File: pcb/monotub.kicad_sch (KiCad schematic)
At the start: 39 parts, among them J1 Barrel_Jack, J2 SCD-40, J3 PROG, J4 FAN, J5 HUMID, J6 WLVL, J7 PUMP, J8 RGB, Q1 NMOS, Q2 NMOS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

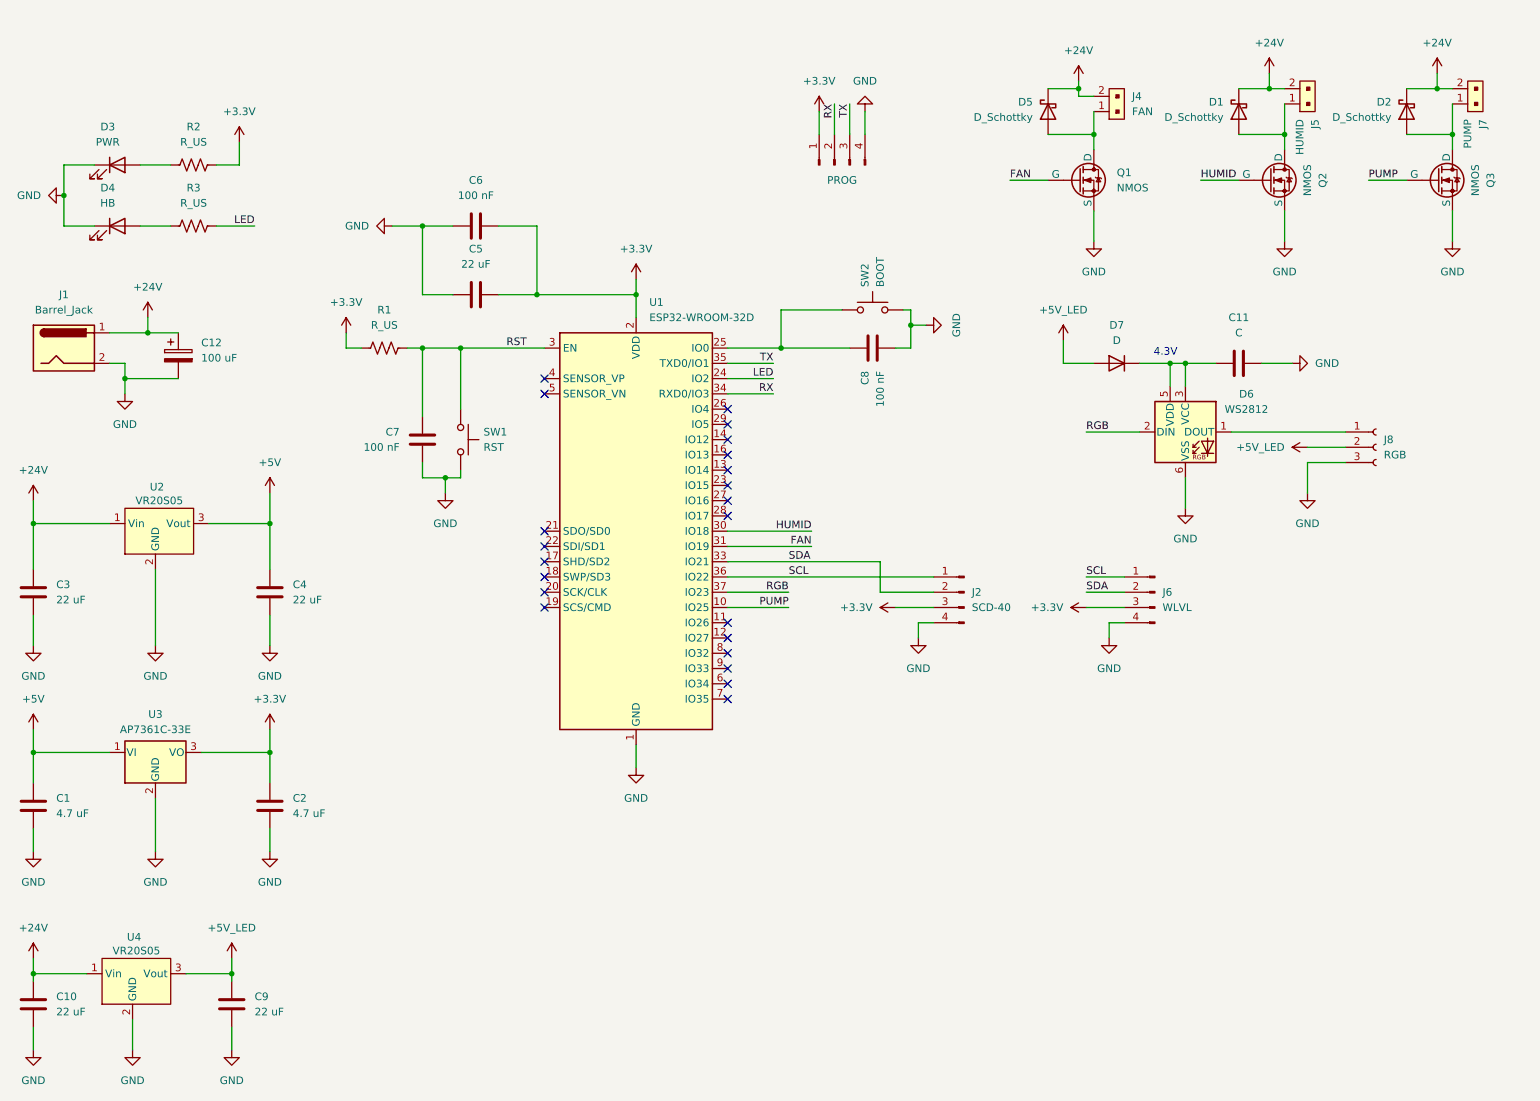
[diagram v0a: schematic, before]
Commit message: Add datasheets, assign footprints, and start PCB file
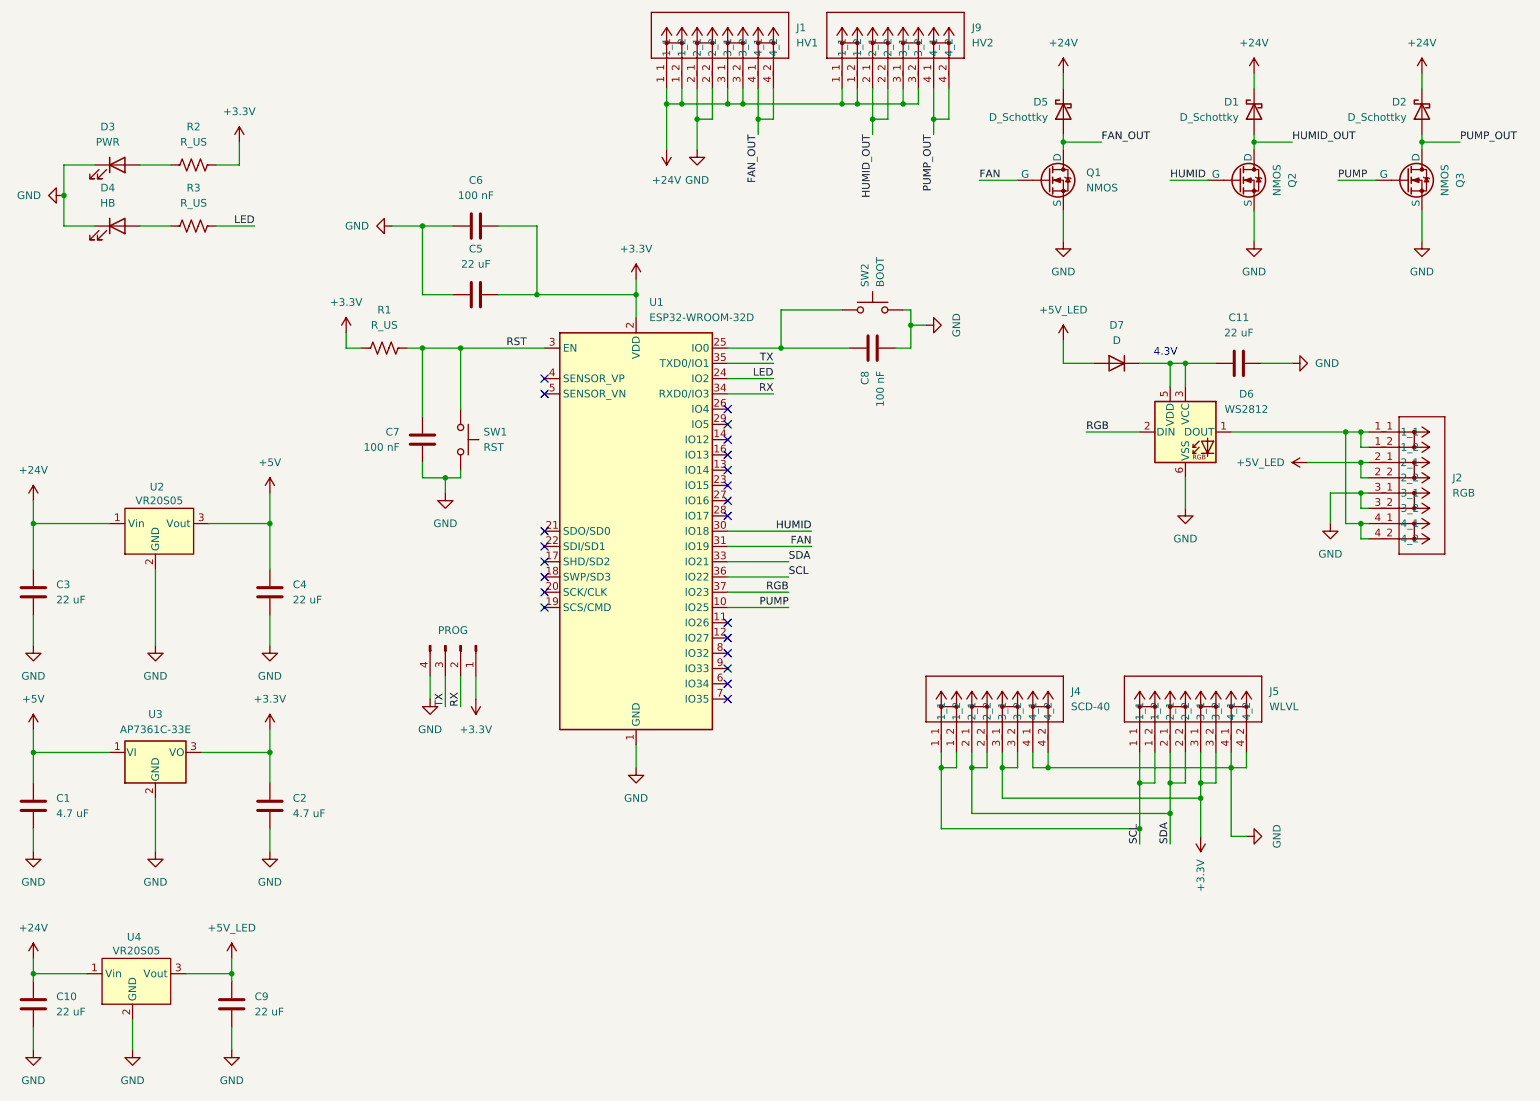
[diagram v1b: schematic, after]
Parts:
- removed C12: 100 uF, symbol Device:C_Polarized
- removed J1: Barrel_Jack, symbol Connector:Barrel_Jack
- removed J2: SCD-40, symbol Connector:Conn_01x04_Pin
- removed J4: FAN, digikey-footprints:PinHeader_1x2_P2mm, symbol dk_Rectangular-Connectors-Headers-Male-Pins:B2B-PH-SM4-TB_LF__SN_
- removed J5: HUMID, digikey-footprints:PinHeader_1x2_P2mm, symbol dk_Rectangular-Connectors-Headers-Male-Pins:B2B-PH-SM4-TB_LF__SN_
- removed J6: WLVL, symbol Connector:Conn_01x04_Pin
- removed J7: PUMP, digikey-footprints:PinHeader_1x2_P2mm, symbol dk_Rectangular-Connectors-Headers-Male-Pins:B2B-PH-SM4-TB_LF__SN_
- removed J8: RGB, symbol Connector:Conn_01x03_Socket
- added J1: HV1, WAGO:CONN_2601-1104_WAG, symbol 2024-05-14_20-07-04:2601-1104
- added J2: RGB, WAGO:CONN_2601-1104_WAG, symbol 2024-05-14_20-07-04:2601-1104
- added J4: SCD-40, WAGO:CONN_2601-1104_WAG, symbol 2024-05-14_20-07-04:2601-1104
- added J5: WLVL, WAGO:CONN_2601-1104_WAG, symbol 2024-05-14_20-07-04:2601-1104
- added J9: HV2, WAGO:CONN_2601-1104_WAG, symbol 2024-05-14_20-07-04:2601-1104
- C1, C10, C2, C3, C4, C5, C6, C7, C8, C9: footprint (none) -> Capacitor_SMD:C_0805_2012Metric_Pad1.18x1.45mm_HandSolder
- C11: value C -> 22 uF; footprint (none) -> Capacitor_SMD:C_0805_2012Metric_Pad1.18x1.45mm_HandSolder
- D1, D2, D5: footprint (none) -> Diode_SMD:D_SMA_Handsoldering
- D3, D4: footprint (none) -> LED_SMD:LED_0805_2012Metric_Pad1.15x1.40mm_HandSolder
- D7: footprint (none) -> Diode_SMD:D_SOD-123
- J3: footprint (none) -> Connector_PinSocket_2.54mm:PinSocket_1x04_P2.54mm_Vertical
- Q1, Q2, Q3: footprint (none) -> Package_TO_SOT_SMD:SOT-23
- R1, R2, R3: footprint (none) -> Resistor_SMD:R_0805_2012Metric_Pad1.20x1.40mm_HandSolder
- SW1, SW2: footprint (none) -> Button_Switch_THT:SW_PUSH_6mm
- U2, U4: footprint (none) -> Connector_PinSocket_2.54mm:PinSocket_1x03_P2.54mm_Vertical
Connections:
- net +24V: now also J1.1_1, J1.1_2, J1.3_1, J1.3_2, J9.1_1, J9.1_2, J9.3_1, J9.3_2
- net +3.3V: now also J4.3_1, J4.3_2, J5.3_1, J5.3_2
- net +5V_LED: now also J2.2_1, J2.2_2
- net GND: now also J1.2_1, J1.2_2, J2.3_1, J2.3_2, J4.4_1, J4.4_2, J5.4_1, J5.4_2
- net SCL: now also J4.1_1, J4.1_2, J5.1_1, J5.1_2
- net SDA: now also J4.2_1, J4.2_2, J5.2_1, J5.2_2
- net at D6.1 (DOUT): now also J2.1_1, J2.1_2, J2.4_1, J2.4_2
- net HUMID_OUT: now reaches D1.2 (A), Q2.1 (D)
- net HUMID_OUT: now also J9.2_1, J9.2_2
- net PUMP_OUT: now reaches D2.2 (A), Q3.1 (D)
- net PUMP_OUT: now also J9.4_1, J9.4_2
- net FAN_OUT: now reaches D5.2 (A), Q1.1 (D)
- net FAN_OUT: now also J1.4_1, J1.4_2
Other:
- moved on the sheet: D1, D2, D5, Q1, Q2, Q3

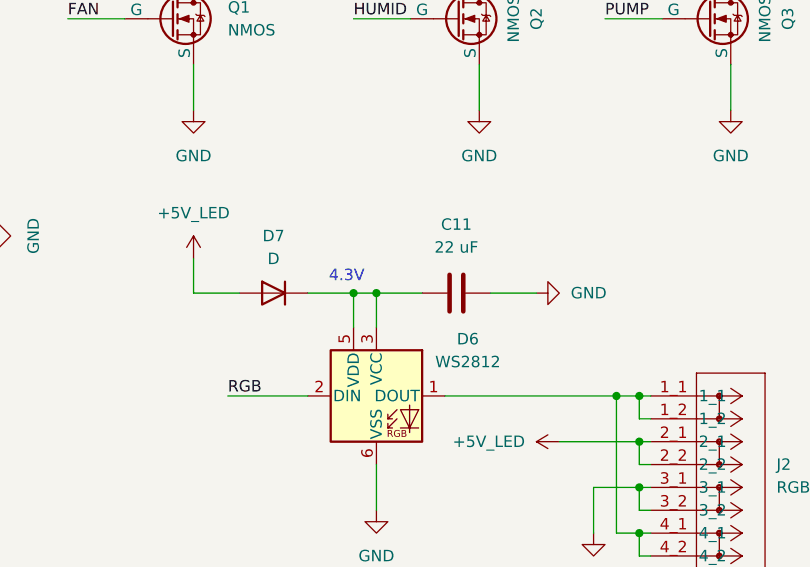
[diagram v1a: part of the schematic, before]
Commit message: Update board with logo and place all components
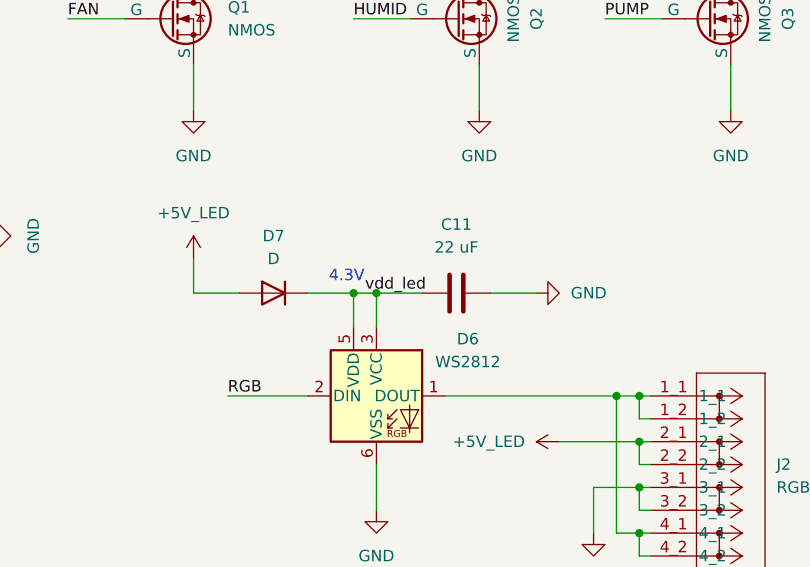
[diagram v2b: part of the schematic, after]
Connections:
- net vdd_led: now reaches C11.1, D6.3 (VCC), D6.5 (VDD), D7.1 (K)
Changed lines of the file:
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@@
+		)
+	)
+	(label "vdd_led"
+		(at 227.33 72.39 0)
+		(fields_autoplaced yes)
+		(effects
+			(font
+				(size 1.27 1.27)
+			)
+			(justify left bottom)
 		)
 	)
